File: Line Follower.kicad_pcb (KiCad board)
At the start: 4 copper layers, 147 x 90 mm, 11 parts, among them J3 Conn_01x04, J4 Conn_01x06, J5 Conn_01x06, U1 Teensy4.1, U2 D42V55F5 5V Voltage Regulator, U3 TB67H420FTG Dual Motor Driver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, U4 Big MOSFET Slide Switch with 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, U5 QTRX-HD-15A

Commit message: Refactor code structure for improved readability and maintainability
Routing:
- net /QTRX12: track 0.00 -> 116.9 mm, vias 0 -> 1
- net /QTRX13: track 0.00 -> 102.8 mm, vias 0 -> 4
- net /QTRX14: track 0.00 -> 102.0 mm
- net /QTRXODD: track 0.00 -> 99.8 mm, vias 0 -> 2
- net /QTRXEVN: track 0.00 -> 94.5 mm, vias 0 -> 1
- net /QTRX11: track 0.00 -> 94.0 mm, vias 0 -> 1
- net /QTRX2: track 0.00 -> 66.8 mm, vias 0 -> 2
- net /QTRX4: track 0.00 -> 56.9 mm, vias 0 -> 1
- net /QTRX6: track 0.00 -> 52.2 mm, vias 0 -> 1
- net +3.3V1: track 0.00 -> 49.5 mm
- net /QTRX8: track 0.00 -> 46.4 mm, vias 0 -> 1
- net /QTRX10: track 0.00 -> 40.3 mm
- net /QTRX15: track 0.00 -> 39.5 mm, vias 0 -> 1
- net /QTRX9: track 0.00 -> 27.9 mm, vias 0 -> 1
- net /QTRX7: track 0.00 -> 26.8 mm, vias 0 -> 1
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- removed copper zone on In1.Cu, net GND

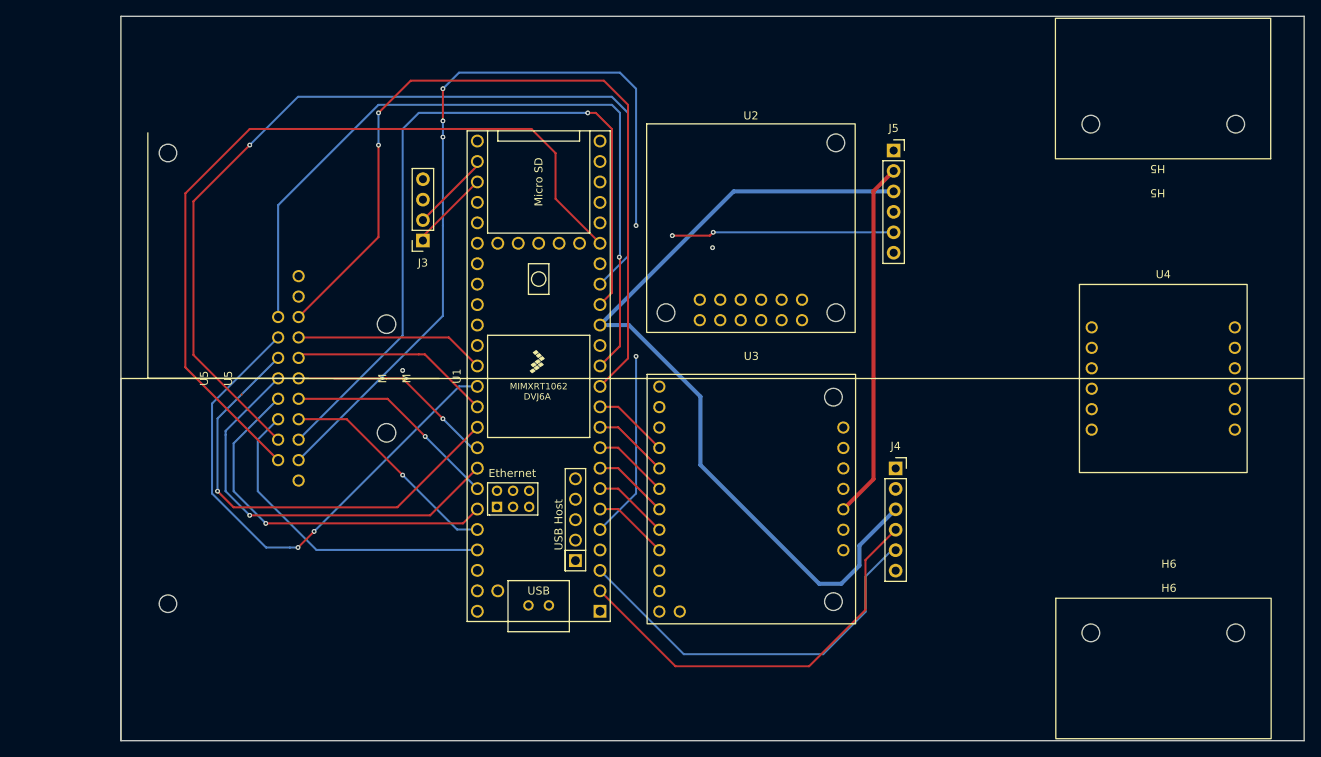
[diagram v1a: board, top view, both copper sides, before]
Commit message: Rectangular Form before deletion
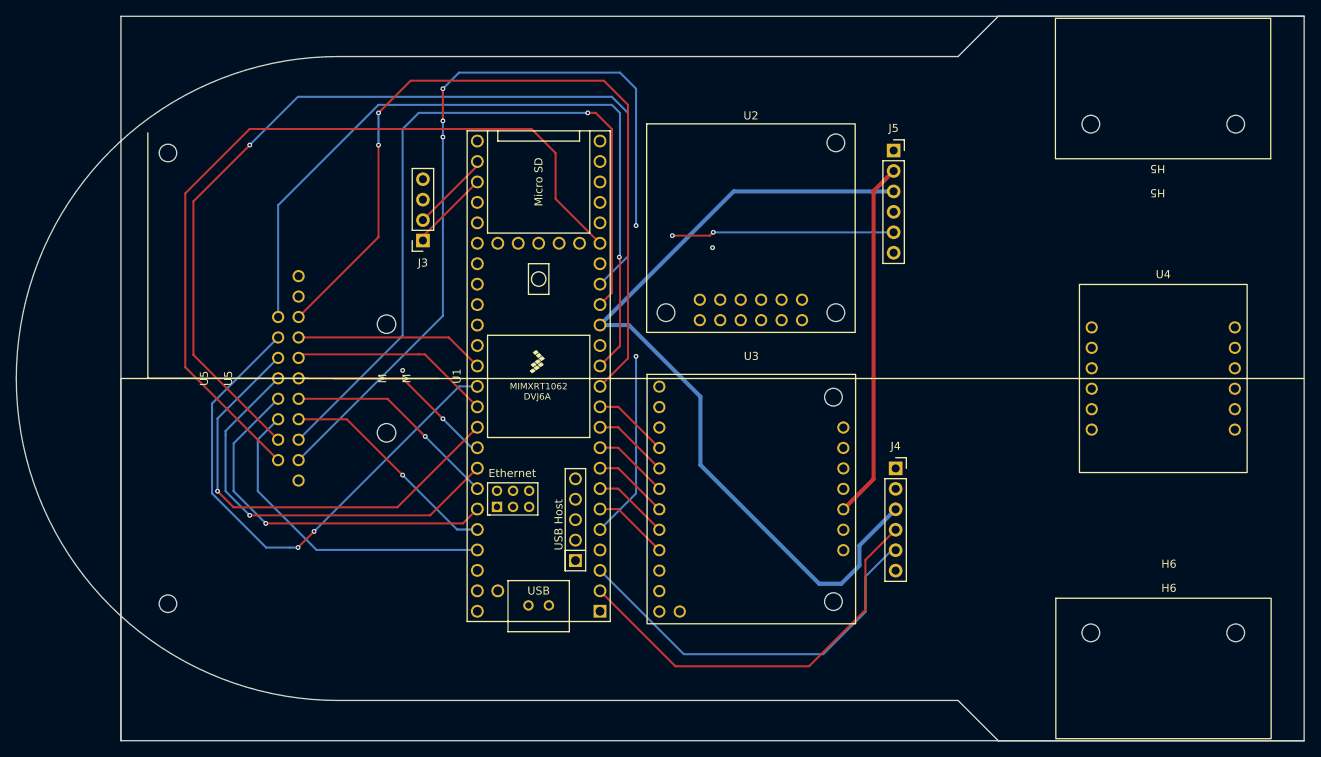
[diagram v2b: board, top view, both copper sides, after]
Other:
- board size 147 x 90 mm -> 160 x 90 mm
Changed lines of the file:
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@@
 		(layer "F.SilkS")
+	)
+	(gr_arc
+		(start 93 132)
+		(mid 53 92)
+		(end 93 52)
+		(stroke
+			(width 0.05)
+			(type default)
+		)
+		(layer "Edge.Cuts")
+	)
+	(gr_line
+		(start 170 132)
+		(end 175 137)
+		(stroke
+			(width 0.05)
+			(type default)
+		)
+		(layer "Edge.Cuts")
+	)
+	(gr_line
+		(start 175 47)
+		(end 213 47)
+		(stroke
+			(width 0.05)
+			(type default)
+		)
+		(layer "Edge.Cuts")
+	)
+	(gr_line
+		(start 93 52)
+		(end 170 52)
+		(stroke
+			(width 0.05)
+			(type default)
+		)
+		(layer "Edge.Cuts")
 	)
 	(gr_rect
@@
 		(layer "Edge.Cuts")
 	)
+	(gr_line
+		(start 93 132)
+		(end 170 132)
+		(stroke
+			(width 0.05)
+			(type default)
+		)
+		(layer "Edge.Cuts")
+	)
+	(gr_line
+		(start 170 52)
+		(end 175 47)
+		(stroke
+			(width 0.05)
+			(type default)
+		)
+		(layer "Edge.Cuts")
+	)
+	(gr_line
+		(start 213 137)
+		(end 175 137)
+		(stroke
+			(width 0.05)
+			(type default)
+		)
+		(layer "Edge.Cuts")
+	)
 	(segment
 		(start 137.92 70.67)
@@
 		(width 0.254)
 		(layer "F.Cu")
-		(net 63)
-	)
-	(segment
-		(start 81 93.9725)
-		(end 81 94)
-		(width 0.254)
-		(layer "F.Cu")

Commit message: Refactor code structure for improved readability and maintainability
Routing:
- net +12V: track 17.6 -> 116.3 mm
- net /QTRX14: track 102.0 -> 98.6 mm
- net /QTRX13: vias 4 -> 3
- added copper zone on In1.Cu, net GND
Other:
- outline, holes or cut-outs redrawn
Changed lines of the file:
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@@
 		(fp_line
 			(start 30.5 -20)
-			(end 30.5 0)
+			(end 30.5 -5)
 			(stroke
 				(width 0.1)
-				(type default)
-			)
-			(layer "F.SilkS")
+				(type solid)
+			)
+			(layer "B.SilkS")
 		)
 		(fp_line
@@
 			(stroke
 				(width 0.1)
-				(type default)
-			)
-			(layer "F.SilkS")
+				(type solid)
+			)
+			(layer "B.SilkS")
 		)
 		(fp_rect
@@
 	)
 	(gr_line
-		(start 66 137)
-		(end 66 92)
+		(start 213 47)
+		(end 213 137)
 		(stroke
-			(width 0.1)
+			(width 0.05)
 			(type default)
 		)
-		(layer "F.SilkS")
-	)
-	(gr_line
-		(start 66 92)
-		(end 213 92)
-		(stroke
-			(width 0.1)
-			(type default)
-		)
-		(layer "F.SilkS")
+		(layer "Edge.Cuts")
 	)
 	(gr_arc
@@
 		(layer "Edge.Cuts")
 	)
-	(gr_rect
-		(start 66 47)
-		(end 213 137)
-		(stroke
-			(width 0.05)
-			(type solid)
-		)
-		(fill no)
-		(layer "Edge.Cuts")
-	)
 	(gr_line
 		(start 93 132)
@@
 	)
 	(segment
-		(start 145.54 87.88)
-		(end 145.54 84.75)
+		(start 192.79 99.79)
+		(end 204.39 88.19)
 		(width 0.508)
 		(layer "In2.Cu")
@@
 	)
 	(segment
+		(start 145.54 82.21)
+		(end 147.75 80)
+		(width 0.508)
+		(layer "In2.Cu")
+		(net 34)
+	)
+	(segment
+		(start 204.39 85.65)
+		(end 198.74 80)
+		(width 0.508)
+		(layer "In2.Cu")
+		(net 34)
+	)
+	(segment
 		(start 155.75 98.09)
-		(end 145.54 87.88)
+		(end 157.45 99.79)
+		(width 0.508)
+		(layer "In2.Cu")
+		(net 34)
+	)
+	(segment
+		(start 147.75 80)
+		(end 198.74 80)
+		(width 0.508)
+		(layer "In2.Cu")
+		(net 34)
+	)
+	(segment
+		(start 157.45 99.79)
+		(end 192.79 99.79)
 		(width 0.508)
 		(layer "In2.Cu")
@@
 	)
 	(via
-		(at 106 62)
-		(size 0.6)
-		(drill 0.3)
-		(layers "F.Cu" "B.Cu")
-		(net 54)
-	)
-	(via
 		(at 130 73)
 		(size 0.6)
@@
 	)
 	(segment
+		(start 111.32 61)
+		(end 82 61)
+		(width 0.254)
+		(layer "F.Cu")
+		(net 57)
+	)
+	(segment
+		(start 82 61)
+		(end 74 69)
+		(width 0.254)
+		(layer "F.Cu")
+		(net 57)
+	)
+	(segment
+		(start 125.52 75.2)
+		(end 111.32 61)
+		(width 0.254)
+		(layer "F.Cu")
+		(net 57)
+	)
+	(segment
+		(start 74 69)
+		(end 74 90.6075)
+		(width 0.254)
+		(layer "F.Cu")
+		(net 57)
+	)
+	(segment
 		(start 74 90.6075)
 		(end 85.5325 102.14)
-		(width 0.254)
-		(layer "F.Cu")
-		(net 57)
-	)
-	(segment
-		(start 82 61)
-		(end 74 69)
-		(width 0.254)
-		(layer "F.Cu")
-		(net 57)
-	)
-	(segment
-		(start 120 64)
-		(end 117 61)
-		(width 0.254)
-		(layer "F.Cu")
-		(net 57)
-	)
-	(segment
-		(start 125.52 75.2)
-		(end 120 69.68)
-		(width 0.254)
-		(layer "F.Cu")
-		(net 57)
-	)
-	(segment
-		(start 117 61)
-		(end 82 61)
-		(width 0.254)
-		(layer "F.Cu")
-		(net 57)
-	)
-	(segment
-		(start 74 69)
-		(end 74 90.6075)
-		(width 0.254)
-		(layer "F.Cu")
-		(net 57)
-	)
-	(segment
-		(start 120 69.68)
-		(end 120 64)
 		(width 0.254)
 		(layer "F.Cu")
@@
 		(net 89)
 	)
+	(zone
+		(net 33)
+		(net_name "GND")
+		(layer "In1.Cu")
+		(hatch edge 0.5)
+		(connect_pads
+			(clearance 0.5)
+		)
+		(min_thickness 0.25)
+		(filled_areas_thickness no)
+		(fill yes
+			(thermal_gap 0.5)
+			(thermal_bridge_width 0.5)
+		)
+		(polygon
+			(pts
+				(xy 213 47) (xy 213 137) (xy 175 137) (xy 170 132) (xy 94 132) (xy 80 123) (xy 80 60) (xy 94 52)
+				(xy 170 52) (xy 175 47)
+			)
+		)
+	)
 	(embedded_fonts no)

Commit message: Refactor code structure for improved readability and maintainability
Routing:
- net +3.3V: track 103.7 -> 99.5 mm
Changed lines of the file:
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@@
 		(attr through_hole)
-		(fp_line
-			(start 61 -20)
-			(end 30.5 -20)
-			(stroke
-				(width 0.1)
-				(type default)
-			)
-			(layer "F.SilkS")
-		)
 		(fp_line
 			(start 30.5 -20)
@@
 	)
 	(segment
-		(start 155.5 117.5)
-		(end 152.75 117.5)
-		(width 0.508)
-		(layer "B.Cu")
-		(net 51)
-	)
-	(segment
-		(start 138 102.75)
-		(end 138 94.25)
-		(width 0.508)
-		(layer "B.Cu")
-		(net 51)
-	)
-	(segment
 		(start 142.125 68.755)
 		(end 162 68.755)
@@
 	)
 	(segment
-		(start 157.75 115.25)
-		(end 155.5 117.5)
+		(start 162.25 108.25)
+		(end 165 105.5)
+		(width 0.508)
+		(layer "B.Cu")
+		(net 51)
+	)
+	(segment
+		(start 165 105.5)
+		(end 165 98)
 		(width 0.508)
 		(layer "B.Cu")
@@
 	)
 	(segment
-		(start 157.75 112.75)
-		(end 157.75 115.25)
+		(start 165 98)
+		(end 154 87)
 		(width 0.508)
 		(layer "B.Cu")
@@
 	)
 	(segment
-		(start 138 94.25)
-		(end 129.11 85.36)
+		(start 127.16 87)
+		(end 125.52 85.36)
 		(width 0.508)
 		(layer "B.Cu")
@@
 	)
 	(segment
-		(start 152.75 117.5)
-		(end 138 102.75)
-		(width 0.508)
-		(layer "B.Cu")
-		(net 51)
-	)
-	(segment
-		(start 162.25 108.25)
-		(end 157.75 112.75)
-		(width 0.508)
-		(layer "B.Cu")
-		(net 51)
-	)
-	(segment
-		(start 129.11 85.36)
-		(end 125.52 85.36)
+		(start 154 87)
+		(end 127.16 87)
 		(width 0.508)
 		(layer "B.Cu")
@@
 		(filled_areas_thickness no)
 		(fill yes
-			(thermal_gap 0.5)
-			(thermal_bridge_width 0.5)
+			(thermal_gap 0.6)
+			(thermal_bridge_width 0.6)
 		)
 		(polygon

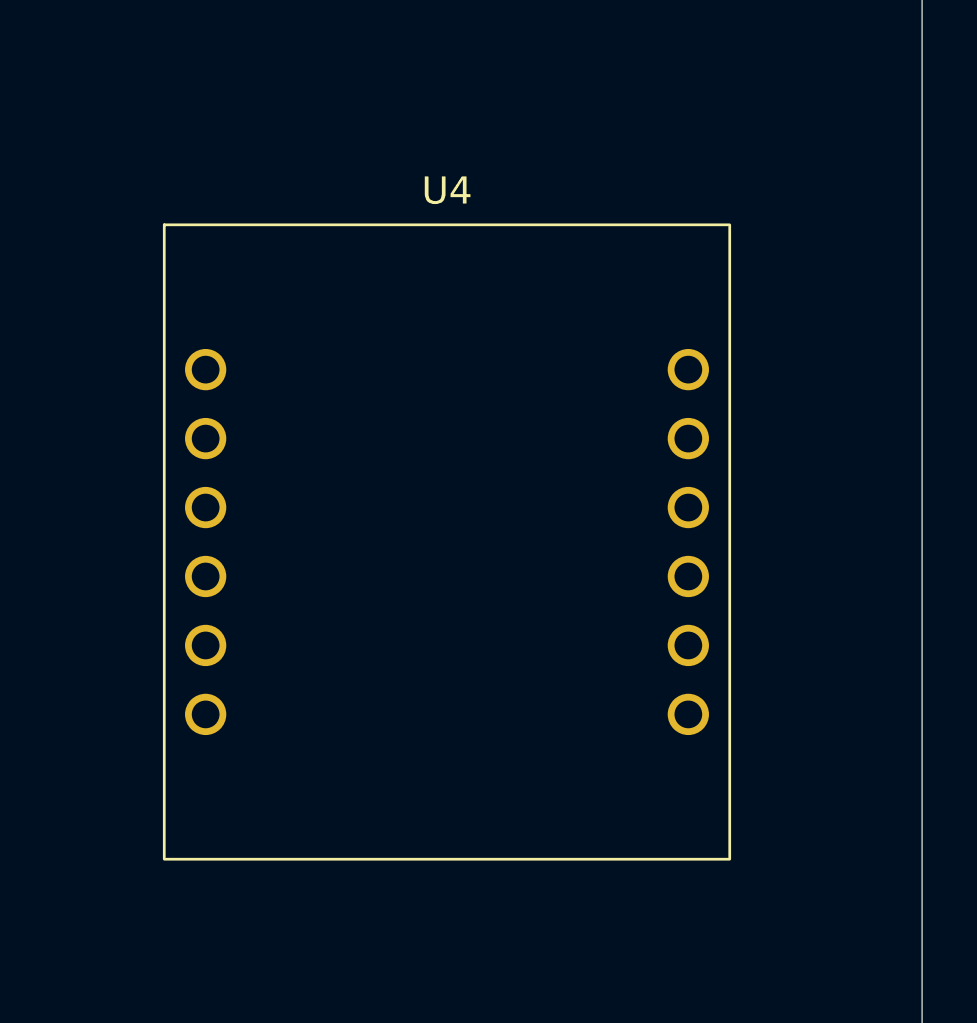
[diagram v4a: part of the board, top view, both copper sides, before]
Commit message: Update active layer in project settings from 2 to 6 for improved design visibility
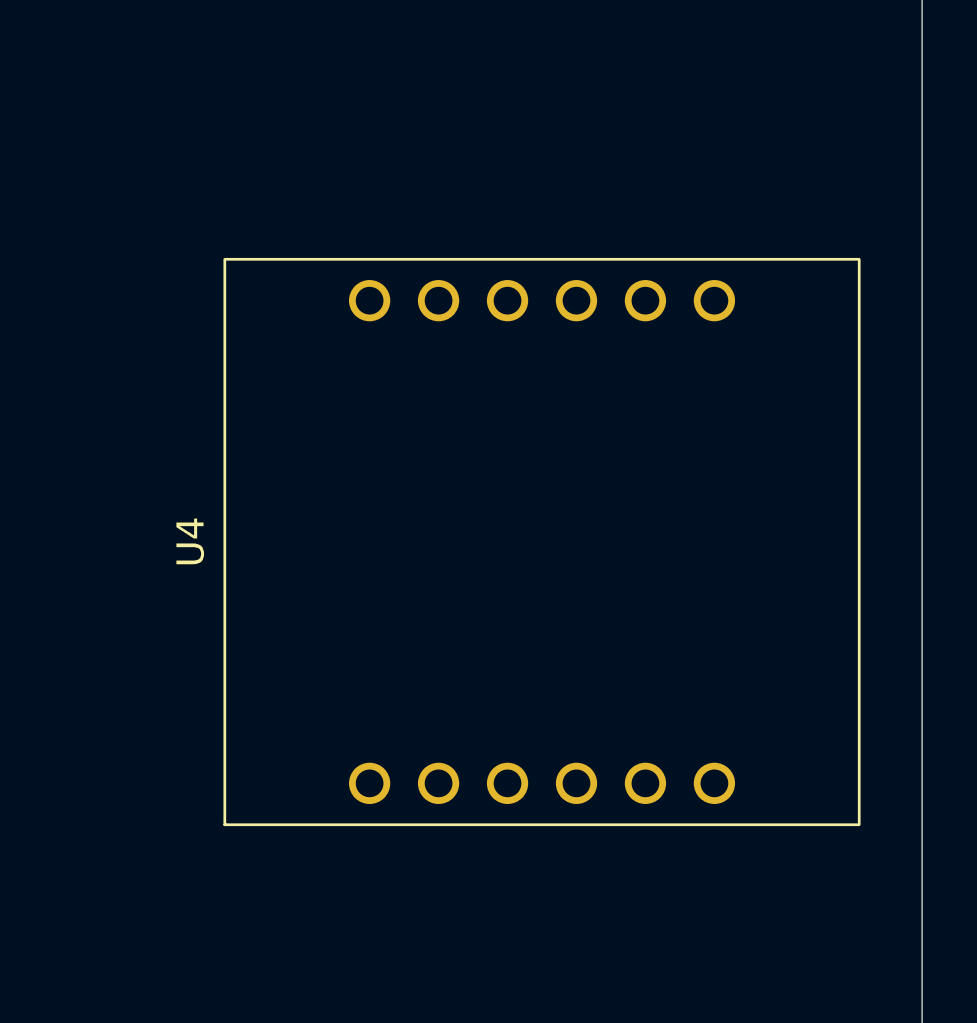
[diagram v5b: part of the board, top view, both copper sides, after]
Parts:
- moved U4 25.1 mm to (210.4, 102.2), turned to 90 degrees
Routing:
- net +12V: track 116.3 -> 96.8 mm
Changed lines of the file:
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@@
 	(footprint "Pololu:Big MOSFET Slide Switch with Reverse Voltage Protection, MP"
 		(layer "F.Cu")
-		(at 185.34 103.43)
+		(at 210.43 102.16 90)
 		(property "Reference" "U4"
-			(at 10.16 -24.36 0)
+			(at 10.16 -24.36 90)
 			(unlocked yes)
 			(layer "F.SilkS")
@@
 		)
 		(property "Value" "Big MOSFET Slide Switch with Reverse Voltage Protection, MP"
-			(at 10.16 -22.86 0)
+			(at 10.16 -22.86 90)
 			(unlocked yes)
 			(layer "F.Fab")
@@
 		)
 		(property "Datasheet" ""
-			(at 0 0 0)
+			(at 0 0 90)
 			(unlocked yes)
 			(layer "F.Fab")
@@
 		)
 		(property "Description" "Big MOSFET Slide Switch with Reverse Voltage Protection, MP"
-			(at 0 0 0)
+			(at 0 0 90)
 			(unlocked yes)
 			(layer "F.Fab")
@@
 		)
 		(fp_text user "${REFERENCE}"
-			(at 10.16 -21.36 0)
+			(at 10.16 -21.36 90)
 			(unlocked yes)
 			(layer "F.Fab")
@@
 		)
 		(pad "1" thru_hole circle
-			(at 1.27 -17.78)
+			(at 1.27 -17.78 90)
 			(size 1.52 1.52)
 			(drill 1.02)
@@
 		)
 		(pad "2" thru_hole circle
-			(at 1.27 -15.24)
+			(at 1.27 -15.24 90)
 			(size 1.52 1.52)
 			(drill 1.02)
@@
 		)
 		(pad "3" thru_hole circle
-			(at 1.27 -12.7)
+			(at 1.27 -12.7 90)
 			(size 1.52 1.52)
 			(drill 1.02)
@@
 		)
 		(pad "4" thru_hole circle
-			(at 1.27 -10.16)
+			(at 1.27 -10.16 90)
 			(size 1.52 1.52)
 			(drill 1.02)
@@
 		)
 		(pad "5" thru_hole circle
-			(at 1.27 -7.62)
+			(at 1.27 -7.62 90)
 			(size 1.52 1.52)
 			(drill 1.02)
@@
 		)
 		(pad "6" thru_hole circle
-			(at 1.27 -5.08)
+			(at 1.27 -5.08 90)
 			(size 1.52 1.52)
 			(drill 1.02)
@@
 		)
 		(pad "7" thru_hole circle
-			(at 19.05 -17.78)
+			(at 19.05 -17.78 90)
 			(size 1.52 1.52)
 			(drill 1.02)
@@
 		)
 		(pad "8" thru_hole circle
-			(at 19.05 -15.24)
+			(at 19.05 -15.24 90)
 			(size 1.52 1.52)
 			(drill 1.02)
@@
 		)
 		(pad "9" thru_hole circle
-			(at 19.05 -12.7)
+			(at 19.05 -12.7 90)
 			(size 1.52 1.52)
 			(drill 1.02)
@@
 		)
 		(pad "10" thru_hole circle
-			(at 19.05 -10.16)
+			(at 19.05 -10.16 90)
 			(size 1.52 1.52)
 			(drill 1.02)
@@
 		)
 		(pad "11" thru_hole circle
-			(at 19.05 -7.62)
+			(at 19.05 -7.62 90)
 			(size 1.52 1.52)
 			(drill 1.02)
@@
 		)
 		(pad "12" thru_hole circle
-			(at 19.05 -5.08)
+			(at 19.05 -5.08 90)
 			(size 1.52 1.52)
 			(drill 1.02)
@@
 	)
 	(segment
-		(start 192.79 99.79)
-		(end 204.39 88.19)
+		(start 183.91 98.09)
+		(end 155.75 98.09)
 		(width 0.508)
 		(layer "In2.Cu")
@@
 	)
 	(segment
-		(start 145.54 82.21)
-		(end 147.75 80)
+		(start 192.65 83.11)
+		(end 189.89 80.35)
 		(width 0.508)
 		(layer "In2.Cu")
@@
 	)
 	(segment
-		(start 204.39 85.65)
-		(end 198.74 80)
+		(start 189.89 80.35)
+		(end 176 80.35)
 		(width 0.508)
 		(layer "In2.Cu")
@@
 	)
 	(segment
-		(start 155.75 98.09)
-		(end 157.45 99.79)
+		(start 148 80.35)
+		(end 147.4 80.35)
 		(width 0.508)
 		(layer "In2.Cu")
@@
 	)
 	(segment
-		(start 147.75 80)
-		(end 198.74 80)
+		(start 147.4 80.35)
+		(end 145.54 82.21)
 		(width 0.508)
 		(layer "In2.Cu")
@@
 	)
 	(segment
-		(start 157.45 99.79)
-		(end 192.79 99.79)
+		(start 195.19 86.81)
+		(end 183.91 98.09)
 		(width 0.508)
 		(layer "In2.Cu")
+		(net 34)
+	)
+	(segment
+		(start 195.19 83.11)
+		(end 195.19 86.81)
+		(width 0.508)
+		(layer "In2.Cu")
+		(net 34)
+	)
+	(segment
+		(start 176 80.35)
+		(end 148 80.35)
+		(width 0.508)
+		(layer "In2.Cu")
